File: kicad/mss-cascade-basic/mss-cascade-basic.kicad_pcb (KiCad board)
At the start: 2 copper layers, 82.6 x 76.2 mm, 93 parts, among them J1 Screw_Terminal_01x02, J10 Screw_Terminal_01x02, J2 SM04B-SRSS, J3 SM04B-SRSS, J4 SM04B-SRSS, J5 8P8C, J6 8P8C, J7 AVR-ISP, J8 Screw_Terminal_01x02, J9 Screw_Terminal_01x02, U1 AP7381-50Y, U2 ATtiny861A-S, U3 74HC4049, U4 AP3012

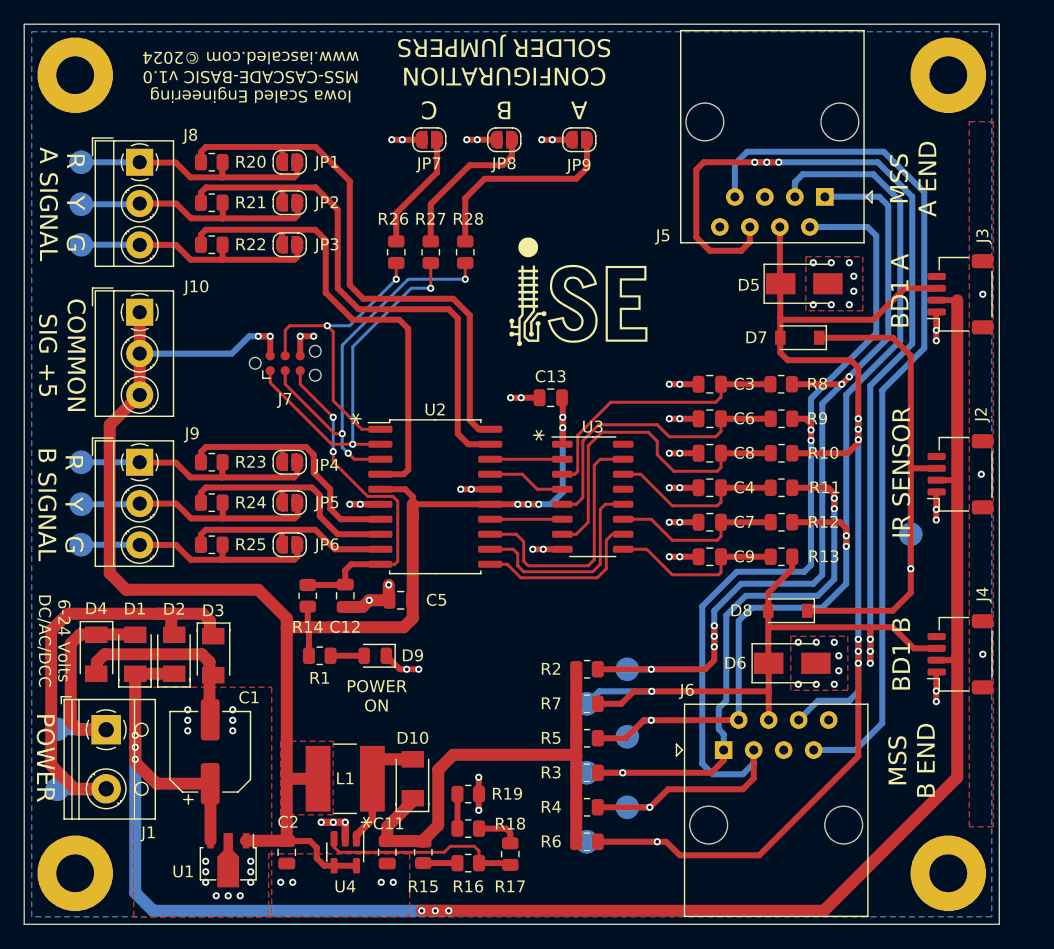
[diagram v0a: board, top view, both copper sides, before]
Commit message: Add test point for 12V, move connectors to align
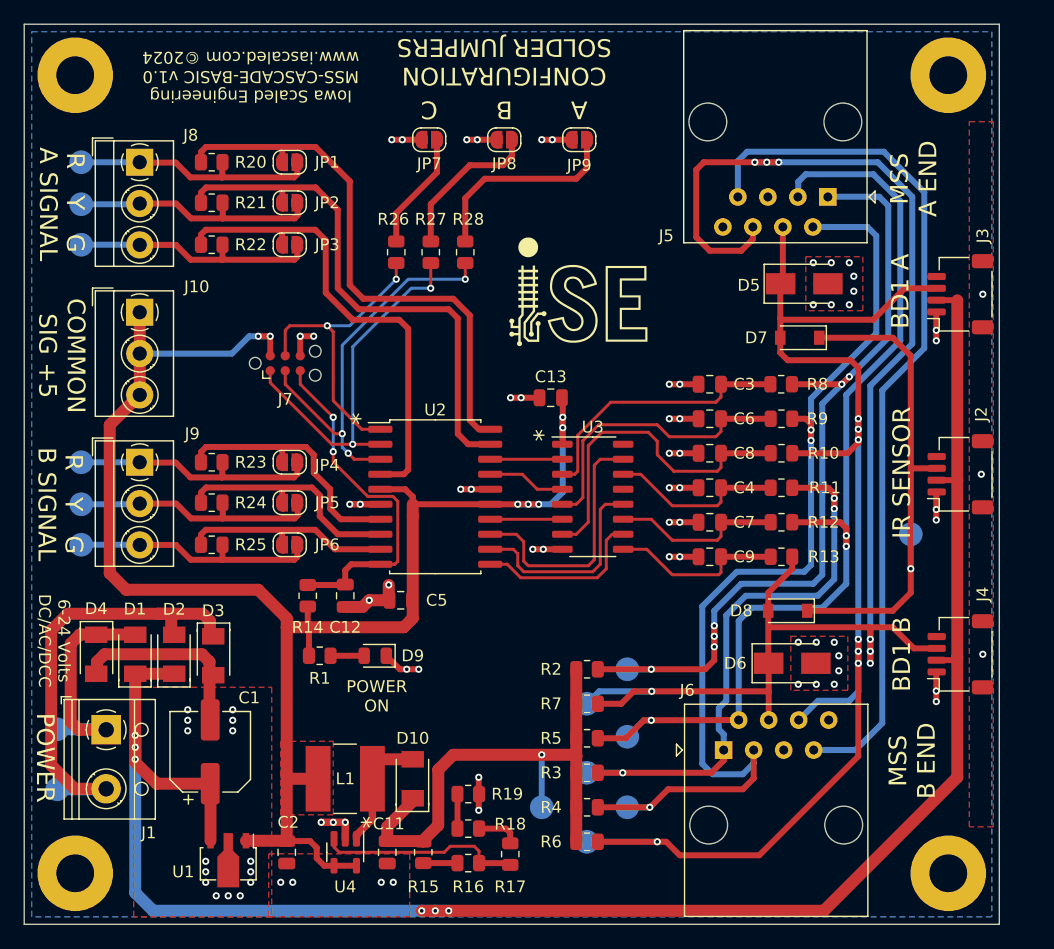
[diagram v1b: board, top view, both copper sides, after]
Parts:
- added TP16: TestPoint, TestPoint:TestPoint_Pad_D2.0mm, B.Cu at (69.2, 181.9)
- moved J5 0.25 mm to (93.4, 130.2)
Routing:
- net +12V: track 55.8 -> 60.2 mm, vias 0 -> 1

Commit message: Update diode footprints on the cascade basic for proper SOD123T on all of the CDBM140Gs Update version to 1.1
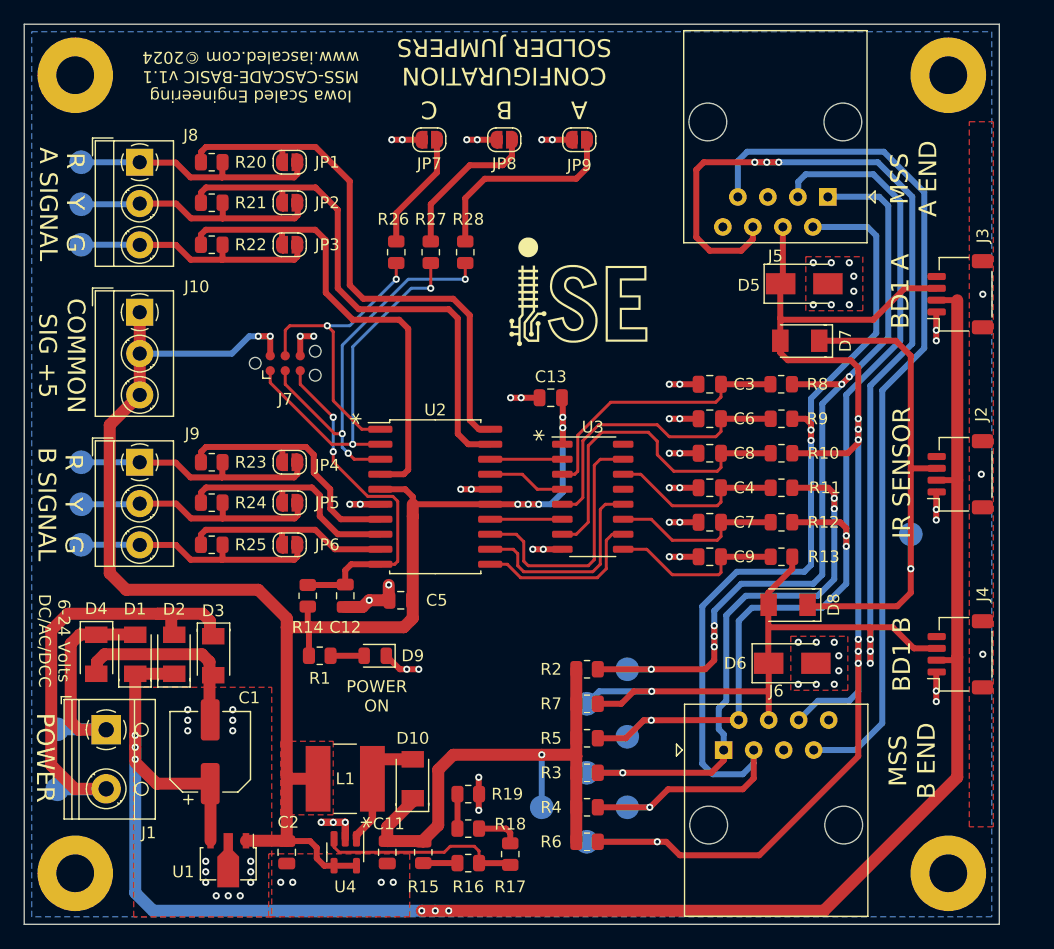
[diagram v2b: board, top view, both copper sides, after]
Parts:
- D7, D8: footprint Diode_SMD:D_SOD-123 -> ISE_Generic:SOD-123T
- moved D8 0.51 mm to (90.1, 164.7)
- moved D7 0.25 mm to (91.1, 142.4)
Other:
- board text added: "Iowa Scaled Engineering MSS-CASCADE-BASIC v1.1 www.iascaled.com ©2024"
- board text removed: "Iowa Scaled Engineering MSS-CASCADE-BASIC v1.0 www.iascaled.com ©2024"

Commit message: Preliminary addition of Atlas signal connectors and the ability to set common anode or cathode
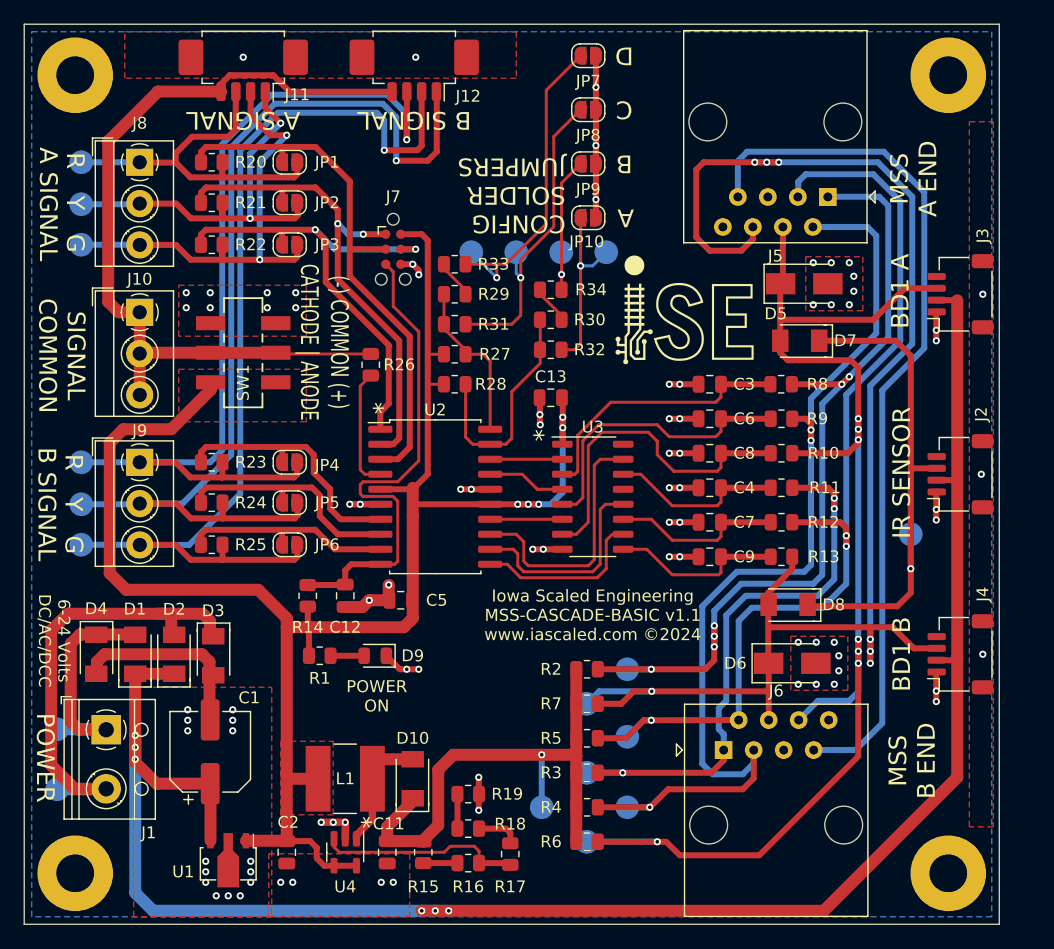
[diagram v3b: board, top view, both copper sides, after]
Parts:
- added J11: Molex 0532610471, Connector_Molex:Molex_PicoBlade_53261-0471_1x04-1MP_P1.25mm_Horizontal, F.Cu at (43.9, 118.9)
- added J12: Molex 0532610471, Connector_Molex:Molex_PicoBlade_53261-0471_1x04-1MP_P1.25mm_Horizontal, F.Cu at (58.4, 118.9)
- added JP10: SolderJumper_2_Open, Jumper:SolderJumper-2_P1.3mm_Open_RoundedPad1.0x1.5mm, F.Cu at (73.2, 132.0)
- added R29: 10k, Resistor_SMD:R_0805_2012Metric, F.Cu at (61.8, 138.4)
- added R30: 10k, Resistor_SMD:R_0805_2012Metric, F.Cu at (70.0, 140.6)
- added R31: 10k, Resistor_SMD:R_0805_2012Metric, F.Cu at (61.8, 141.0)
- added R32: 10k, Resistor_SMD:R_0805_2012Metric, F.Cu at (70.0, 143.1)
- added R33: 10k, Resistor_SMD:R_0805_2012Metric, F.Cu at (61.8, 135.9)
- added R34: 10k, Resistor_SMD:R_0805_2012Metric, F.Cu at (70.0, 138.0)
- added SW1: JS202011SCQN, ISE_UltraLibrarian:SW_JS202011SCQN, F.Cu at (43.9, 143.4)
- added TP17: TestPoint, TestPoint:TestPoint_Pad_D2.0mm, B.Cu at (67.1, 134.9)
- added TP18: TestPoint, TestPoint:TestPoint_Pad_D2.0mm, B.Cu at (74.7, 134.9)
- added TP19: TestPoint, TestPoint:TestPoint_Pad_D2.0mm, B.Cu at (63.2, 134.9)
- added TP20: TestPoint, TestPoint:TestPoint_Pad_D2.0mm, B.Cu at (70.9, 134.9)
- R26, R27, R28: value 1k -> 10k
- moved JP7 15.2 mm to (73.2, 118.2), turned to 0 degrees
- moved J7 13.3 mm to (56.6, 134.6), turned to -90 degrees
- moved R28 11.2 mm to (61.8, 146.1), turned to 180 degrees
- moved R26 9.77 mm to (54.7, 144.4), turned to -90 degrees
- moved R27 8.87 mm to (61.8, 143.5), turned to 180 degrees
- moved JP8 7.55 mm to (73.2, 122.8), turned to 0 degrees
- moved JP9 2.17 mm to (73.2, 127.4), turned to 0 degrees
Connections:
- J10 pad 1: +5V -> Net-(J10-Pad1)
- J10 pad 2: +5V -> Net-(J10-Pad1)
- J10 pad 3: +5V -> Net-(J10-Pad1)
- J7 pad 1: Net-(J7-Pad1) -> /A_SIGNAL_Y
- J7 pad 3: Net-(J7-Pad3) -> /A_SIGNAL_R
- J7 pad 4: Net-(J7-Pad4) -> /A_SIGNAL_G
- JP7 pad 1: Net-(JP7-Pad1) -> Net-(TP19-Pad1)
- R26 pad 1: Net-(J7-Pad4) -> Net-(J10-Pad1)
- R26 pad 2: Net-(JP7-Pad1) -> /COM_SENSE
- R27 pad 1: Net-(J7-Pad1) -> /OPTIONS_1
- R27 pad 2: Net-(JP8-Pad1) -> +5V
- R28 pad 1: Net-(J7-Pad3) -> /OPTIONS_2
- R28 pad 2: Net-(JP9-Pad1) -> +5V
- U2 pad 1: Net-(J7-Pad4) -> /A_SIGNAL_G
- U2 pad 19: /A_SIGNAL_Y -> /OPTIONS_2
- U2 pad 2: Net-(J7-Pad1) -> /A_SIGNAL_Y
- U2 pad 20: /A_SIGNAL_R -> /OPTIONS_1
- U2 pad 3: Net-(J7-Pad3) -> /A_SIGNAL_R
- U2 pad 4: /A_SIGNAL_G -> /COM_SENSE
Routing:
- net Net-(J10-Pad1): track 0.00 -> 69.9 mm
- net Net-(J9-Pad2): track 21.2 -> 85.2 mm, vias 0 -> 1
- net Net-(JP6-Pad2): track 21.2 -> 84.8 mm, vias 0 -> 1
- net Net-(JP4-Pad2): track 21.2 -> 78.8 mm, vias 0 -> 1
- net Net-(J7-Pad3): track 34.1 -> 0.00 mm, vias 3 -> 0
- net Net-(J7-Pad1): track 31.5 -> 0.00 mm, vias 2 -> 0
- net Net-(TP19-Pad1): track 0.00 -> 27.9 mm, vias 0 -> 1
- net Net-(J7-Pad4): track 26.3 -> 0.00 mm, vias 2 -> 0
- net /OPTIONS_2: track 0.00 -> 19.9 mm
- net Net-(JP3-Pad2): track 21.2 -> 38.5 mm, vias 0 -> 2
- net Net-(JP10-Pad1): track 0.00 -> 15.2 mm, vias 0 -> 1
- net /OPTIONS_1: track 0.00 -> 13.9 mm
- net Net-(JP8-Pad1): track 13.1 -> 26.8 mm, vias 0 -> 1
- net +5V: track 140.6 -> 153.9 mm, vias 7 -> 5
- net Net-(J8-Pad2): track 21.2 -> 33.6 mm, vias 0 -> 2
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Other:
- board text added: "(-) COMMON (+)"
- board text added: "CATHODE | ANODE"
- board text added: "CONFIG SOLDER JUMPERS"
- board text added: "D"
- board text added: "SIGNAL COMMON"
- board text removed: "COMMON SIG +5"
- board text removed: "CONFIGURATION SOLDER JUMPERS"

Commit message: A few cleanup things
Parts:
- moved C13 1.59 mm to (68.6, 148.0), turned to 90 degrees
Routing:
- net /A_ADJACENT: track 115.6 -> 108.1 mm
- net +5V: track 153.9 -> 149.2 mm, vias 5 -> 0
- net Net-(J5-Pad2): track 88.0 -> 86.7 mm
- net Net-(J6-Pad1): track 49.2 -> 48.4 mm

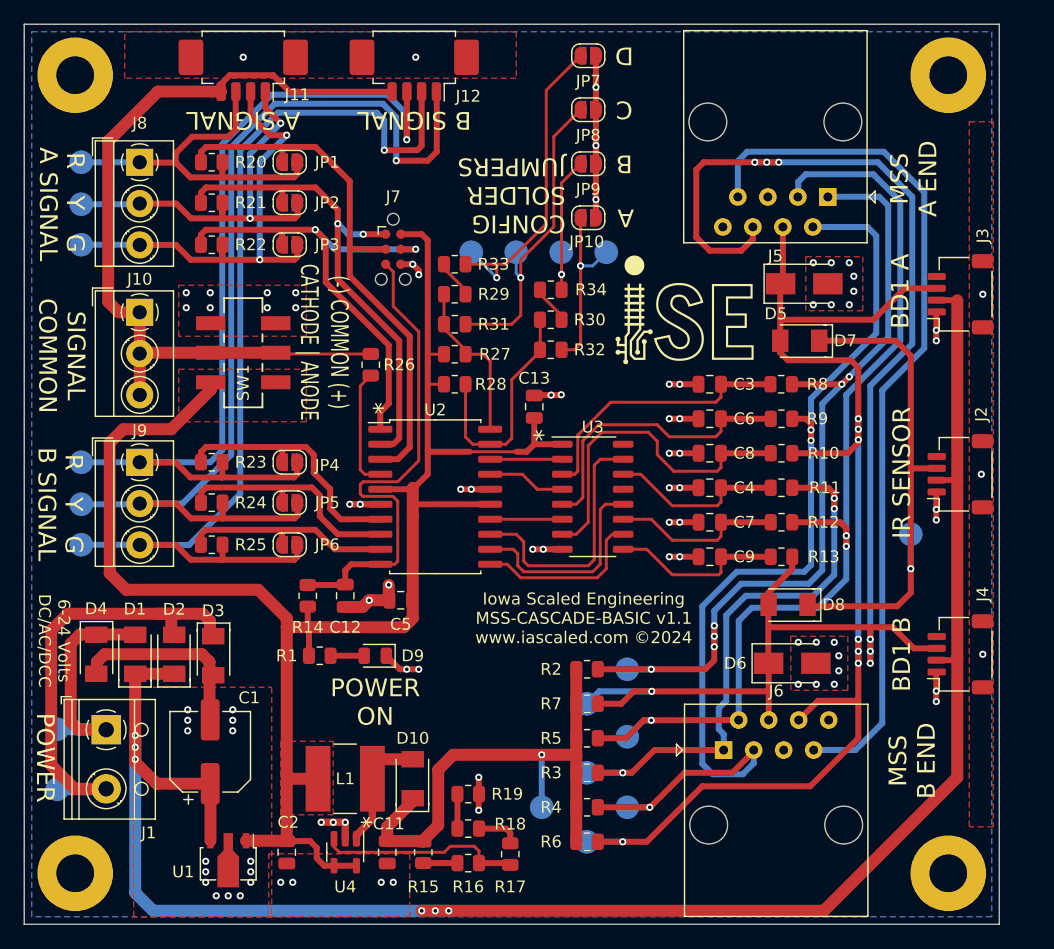
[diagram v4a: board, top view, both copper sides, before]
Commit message: Change text, add test point for common
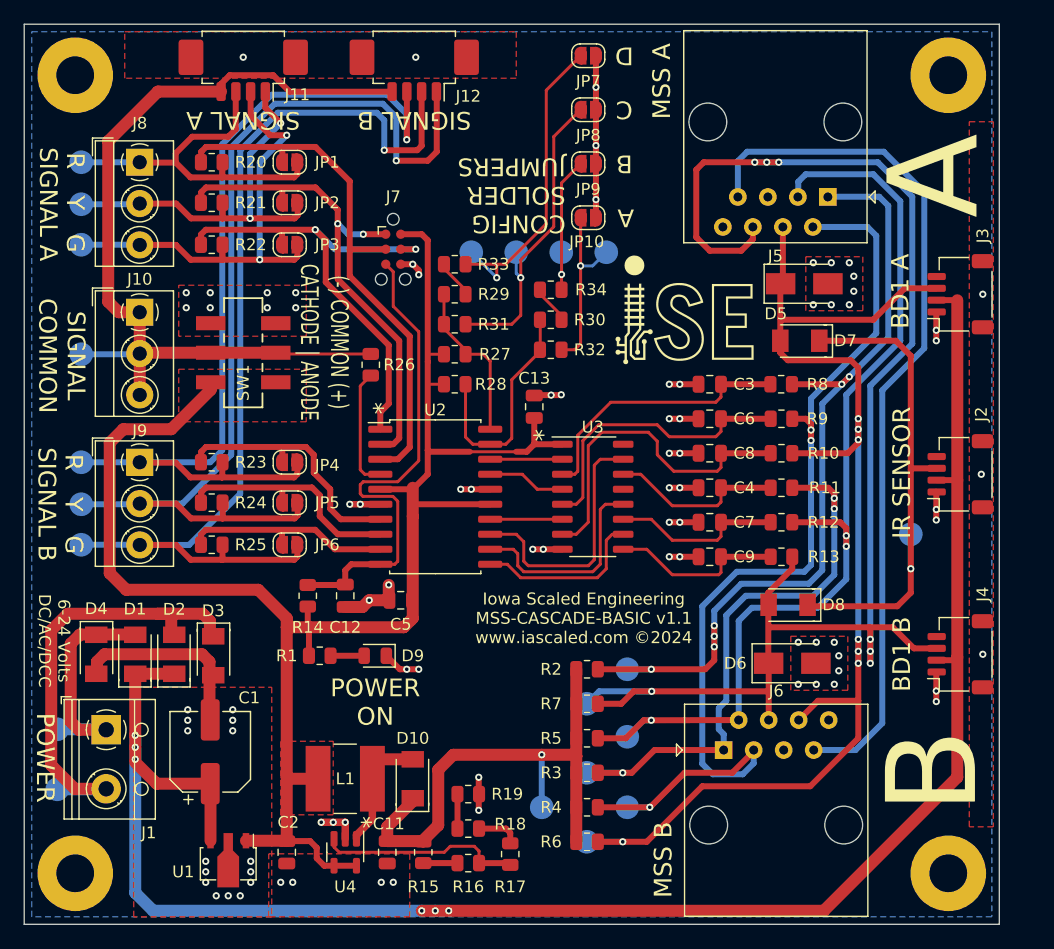
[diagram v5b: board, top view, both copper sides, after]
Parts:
- added TP21: TestPoint, TestPoint:TestPoint_Pad_D2.0mm, B.Cu at (30.2, 143.5)
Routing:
- net Net-(J10-Pad1): track 69.9 -> 74.9 mm
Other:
- board text added: "MSS A"
- board text added: "MSS B"
- board text added: "SIGNAL A"
- board text added: "SIGNAL B"
- board text removed: "A SIGNAL"
- board text removed: "B SIGNAL"
- board text removed: "MSS A END"
- board text removed: "MSS B END"
